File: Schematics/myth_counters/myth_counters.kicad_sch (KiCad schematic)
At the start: 9 parts, among them U1 74LS08, U2 74LS08, U3 4072, U4 74HC74, U5 74HC02, U6 74HC00, U7 74LS32, U8 74HC193, U9 74HC193

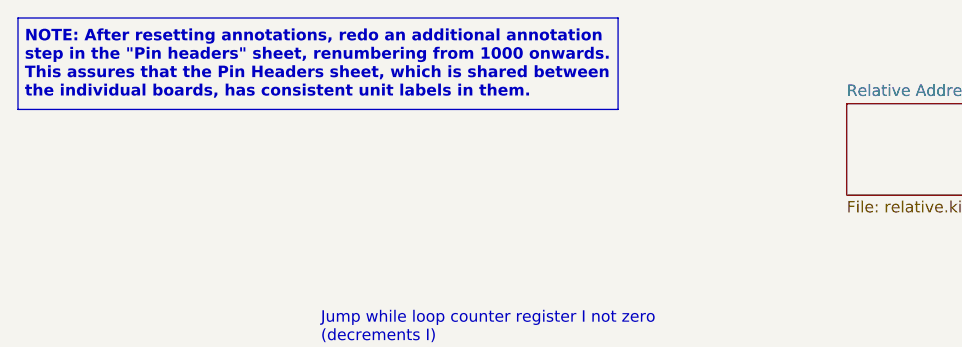
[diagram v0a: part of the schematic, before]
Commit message: Reduce number of shared headers
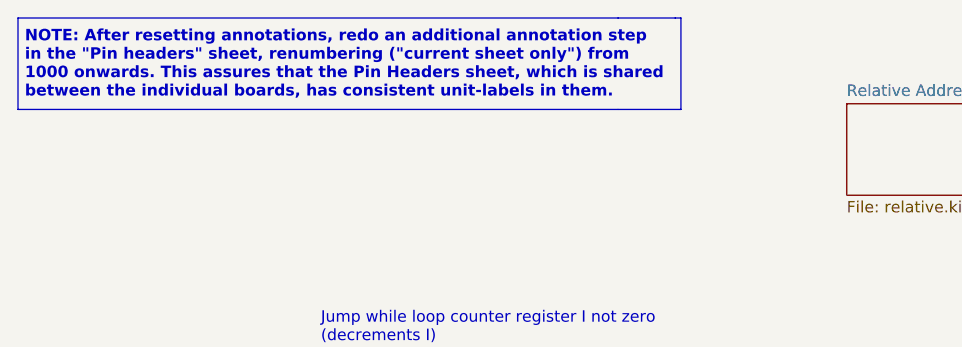
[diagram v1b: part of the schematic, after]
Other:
- note added: "NOTE: After resetting annotations, redo an additional annotation step in the "Pin headers" sheet, renumbering ("current sheet only") from 1000 onwards. This assures that the Pin Headers sheet, which is shared between the individual boards, has consistent unit-labels in them."
- note removed: "NOTE: After resetting annotations, redo an additional annotation step in the "Pin headers" sheet, renumbering from 1000 onwards. This assures that the Pin Headers sheet, which is shared between the individual boards, has consistent unit labels in them."
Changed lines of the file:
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@@
+		)
+	)
+	(polyline
+		(pts
+			(xy 81.28 24.765) (xy 88.265 24.765)
+		)
+		(stroke
+			(width 0)
+			(type default)
 		)
 	)
@@
 		)
 	)
+	(polyline
+		(pts
+			(xy 81.28 14.605) (xy 87.63 14.605)
+		)
+		(stroke
+			(width 0)
+			(type default)
+		)
+	)
 	(bus
 		(pts
@@
 	(polyline
 		(pts
-			(xy 81.28 14.605) (xy 81.28 24.765)
+			(xy 88.265 14.605) (xy 88.265 24.765)
 		)
 		(stroke
@@
 		(pts
 			(xy 59.69 68.58) (xy 45.72 68.58)
+		)
+		(stroke
+			(width 0)
+			(type default)
+		)
+	)
+	(polyline
+		(pts
+			(xy 87.63 14.605) (xy 88.265 14.605)
 		)
 		(stroke
@@
 		)
 	)
-	(text "NOTE: After resetting annotations, redo an additional annotation\nstep in the \"Pin headers\" sheet, renumbering from 1000 onwards.\nThis assures that the Pin Headers sheet, which is shared between\nthe individual boards, has consistent unit labels in them."
+	(text "NOTE: After resetting annotations, redo an additional annotation step\nin the \"Pin headers\" sheet, renumbering (\"current sheet only\") from\n1000 onwards. This assures that the Pin Headers sheet, which is shared\nbetween the individual boards, has consistent unit-labels in them."
 		(exclude_from_sim no)
 		(at 15.367 23.622 0)

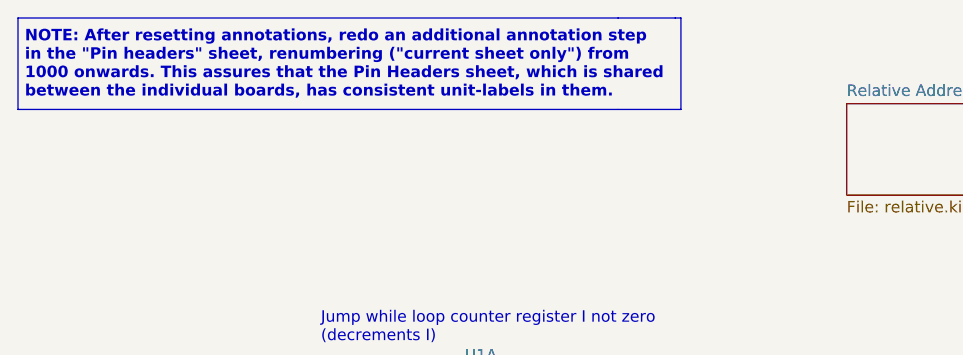
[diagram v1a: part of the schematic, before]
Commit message: Improve schematics for readability
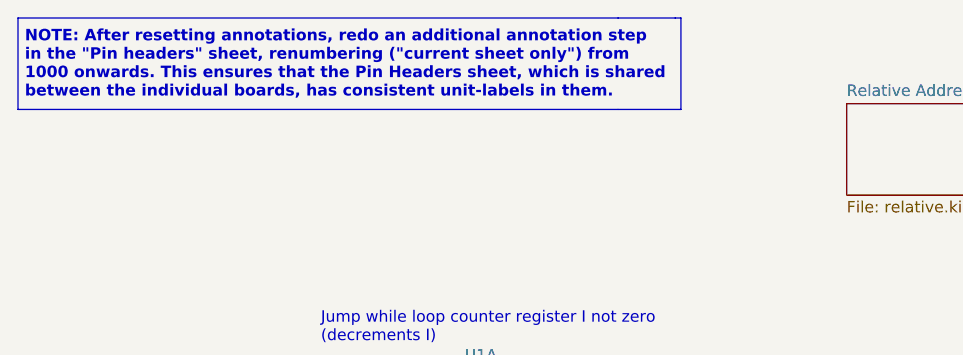
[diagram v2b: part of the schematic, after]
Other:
- note added: "NOTE: After resetting annotations, redo an additional annotation step in the "Pin headers" sheet, renumbering ("current sheet only") from 1000 onwards. This ensures that the Pin Headers sheet, which is shared between the individual boards, has consistent unit-labels in them."
- note removed: "NOTE: After resetting annotations, redo an additional annotation step in the "Pin headers" sheet, renumbering ("current sheet only") from 1000 onwards. This assures that the Pin Headers sheet, which is shared between the individual boards, has consistent unit-labels in them."
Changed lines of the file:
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@@
 		)
 	)
-	(text "NOTE: After resetting annotations, redo an additional annotation step\nin the \"Pin headers\" sheet, renumbering (\"current sheet only\") from\n1000 onwards. This assures that the Pin Headers sheet, which is shared\nbetween the individual boards, has consistent unit-labels in them."
+	(text "NOTE: After resetting annotations, redo an additional annotation step\nin the \"Pin headers\" sheet, renumbering (\"current sheet only\") from\n1000 onwards. This ensures that the Pin Headers sheet, which is shared\nbetween the individual boards, has consistent unit-labels in them."
 		(exclude_from_sim no)
 		(at 15.367 23.622 0)

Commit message: Change d to g
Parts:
- added C1001: C 100nF, Capacitor_THT:C_Disc_D5.0mm_W2.5mm_P2.50mm, symbol Device:C_Small
- added C1002: CP 10μF, Capacitor_THT:CP_Radial_D6.3mm_P2.50mm, symbol Device:C_Polarized_Small
- U1, U2, U3, U4, U5, U6, U7: footprint (none) -> Package_DIP:DIP-14_W7.62mm_LongPads
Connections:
- net +5V: now also C1001.1, C1002.1
- net GND: now also C1001.2, C1002.2

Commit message: Change semantics of xB
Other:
- sheet Relative Addressing Switch renamed Addressing Switch
- sheet Addressing Switch: file relative.kicad_sch -> addr.kicad_sch
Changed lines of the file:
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@@
 			(color 0 0 0 0.0000)
 		)
-		(property "Sheetname" "Relative Addressing Switch"
+		(property "Sheetname" "Addressing Switch"
 			(at 106.68 23.4184 0)
 			(effects
@@
 			)
 		)
-		(property "Sheetfile" "relative.kicad_sch"
+		(property "Sheetfile" "addr.kicad_sch"
 			(at 106.68 34.8746 0)
 			(effects

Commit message: Change signal names
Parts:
- removed unit 4 of U2
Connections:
- net JUMP: now also U6.1
- net xW_pre renamed xJWIT_pre
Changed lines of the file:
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@@
-	(wire
-		(pts
-			(xy 135.89 63.5) (xy 153.67 63.5)
-		)
-		(stroke
-			(width 0)
-			(type default)
-		)
-	)
 	(wire
 		(pts
@@
 	(wire
 		(pts
+			(xy 138.43 60.96) (xy 168.91 60.96)
+		)
+		(stroke
+			(width 0)
+			(type default)
+		)
+	)
+	(wire
+		(pts
 			(xy 59.69 78.74) (xy 59.69 68.58)
 		)
@@
 	(wire
 		(pts
-			(xy 135.89 63.5) (xy 125.73 73.66)
+			(xy 125.73 73.66) (xy 138.43 60.96)
 		)
 		(stroke
@@
 		)
 	)
-	(global_label "xW_pre"
+	(global_label "xJWIT_pre"
 		(shape input)
 		(at 45.72 63.5 180)
@@
 		(property "Intersheetrefs" "${INTERSHEET_REFS}"
 			(at 124.0148 137.16 0)
-			(effects
-				(font
-					(size 1.27 1.27)
-				)
-				(justify right)
-				(hide yes)
-			)
-		)
-	)
-	(global_label "xB"
-		(shape input)
-		(at 153.67 58.42 180)
-		(fields_autoplaced yes)
-		(effects
-			(font
-				(size 1.27 1.27)
-			)
-			(justify right)
-		)
-		(property "Intersheetrefs" "${INTERSHEET_REFS}"
-			(at 148.3867 58.42 0)
 			(effects
 				(font
@@
 				)
 			)
-		)
-	)
-	(symbol
-		(lib_id "74xx:74LS08")
-		(at 161.29 60.96 0)
-		(unit 4)
-		(exclude_from_sim no)
-		(in_bom yes)
-		(on_board yes)
-		(dnp no)
-		(fields_autoplaced yes)
-		(property "Reference" "U2"
-			(at 161.2817 52.07 0)
-			(effects
-				(font
-					(size 1.27 1.27)
-				)
-			)
-		)
-		(property "Value" "74LS08"
-			(at 161.2817 54.61 0)
-			(effects
-				(font
-					(size 1.27 1.27)
-				)
-			)
-		)
-		(property "Footprint" "Package_DIP:DIP-14_W7.62mm_LongPads"
-			(at 161.29 60.96 0)
-			(effects
-				(font
-					(size 1.27 1.27)
-				)
-				(hide yes)
-			)
-		)
-		(property "Datasheet" "http://www.ti.com/lit/gpn/sn74LS08"
-			(at 161.29 60.96 0)
-			(effects
-				(font
-					(size 1.27 1.27)
-				)
-				(hide yes)
-			)
-		)
-		(property "Description" "Quad And2"
-			(at 161.29 60.96 0)
-			(effects
-				(font
-					(size 1.27 1.27)
-				)
-				(hide yes)
-			)
-		)
-		(pin "8"
-		)
-		(pin "2"
-		)
-		(pin "9"
-		)
-		(pin "11"
-		)
-		(pin "12"
-		)
-		(pin "13"
-		)
-		(pin "14"
-		)
-		(pin "7"
-		)
-		(pin "3"
-		)
-		(pin "1"
-		)
-		(pin "5"
-		)
-		(pin "4"
-		)
-		(pin "10"
-		)
-		(pin "6"
-		)
-		(instances
-			(project "myth_counters"
-				(path "/c50a2a1f-7d02-4e47-8cba-362a907cb5f7"
-					(reference "U2")
-					(unit 4)
-				)
-			)
